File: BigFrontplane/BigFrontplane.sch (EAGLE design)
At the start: 7 parts

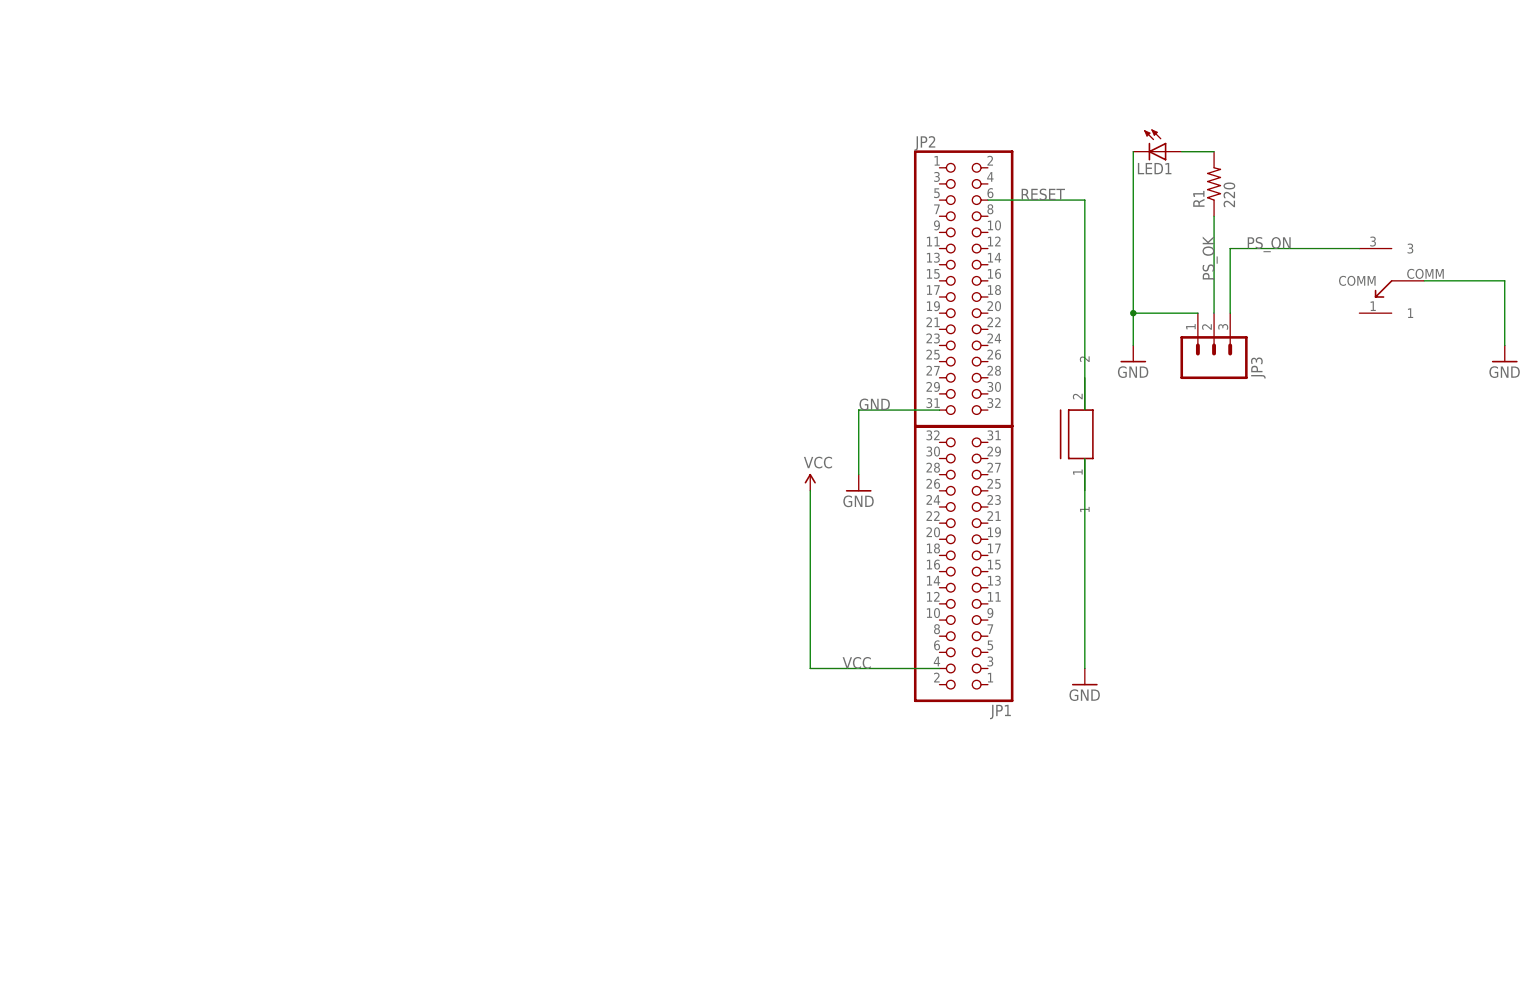
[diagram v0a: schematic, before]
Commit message: Updated Front Panel
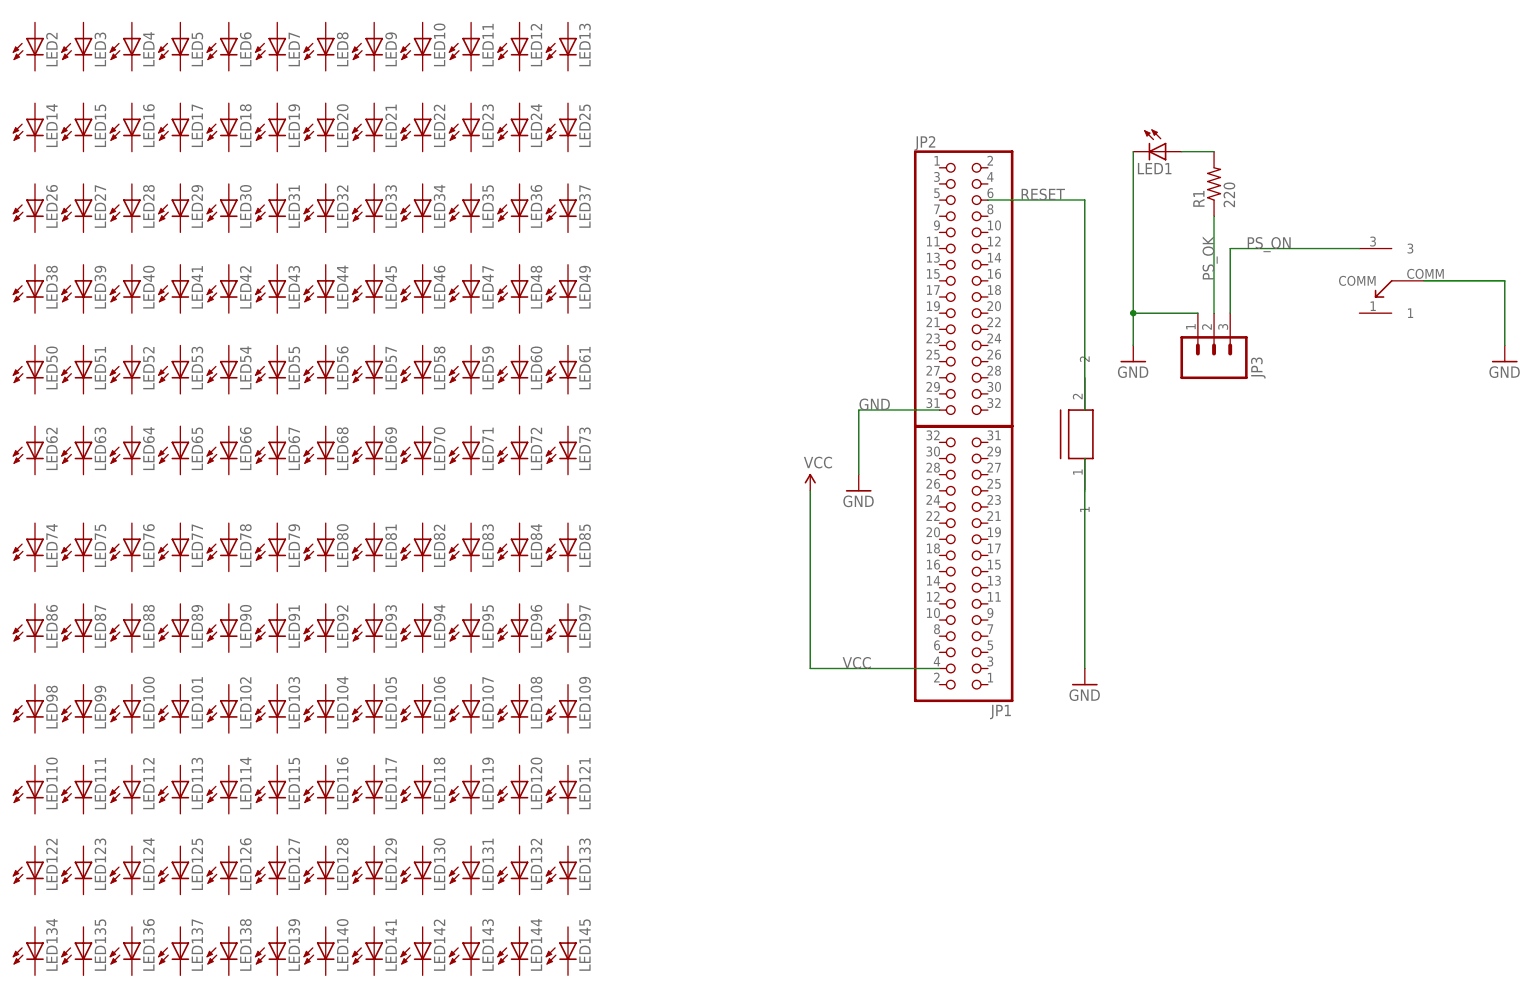
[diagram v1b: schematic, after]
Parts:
- added LED10, LED100, LED101, LED102, LED103, LED104, LED105, LED106, LED107, LED108, LED109, LED11, LED110, LED111, LED112, LED113, LED114, LED115, LED116, LED117, LED118, LED119, LED12, LED120, LED121, LED122, LED123, LED124, LED125, LED126, LED127, LED128, LED129, LED13, LED130, LED131, LED132, LED133, LED134, LED135, LED136, LED137, LED138, LED139, LED14, LED140, LED141, LED142, LED143, LED144, LED145, LED15, LED16, LED17, LED18, LED19, LED2, LED20, LED21, LED22, LED23, LED24, LED25, LED26, LED27, LED28, LED29, LED3, LED30, LED31, LED32, LED33, LED34, LED35, LED36, LED37, LED38, LED39, LED4, LED40, LED41, LED42, LED43, LED44, LED45, LED46, LED47, LED48, LED49, LED5, LED50, LED51, LED52, LED53, LED54, LED55, LED56, LED57, LED58, LED59, LED6, LED60, LED61, LED62, LED63, LED64, LED65, LED66, LED67, LED68, LED69, LED7, LED70, LED71, LED72, LED73, LED74, LED75, LED76, LED77, LED78, LED79, LED8, LED80, LED81, LED82, LED83, LED84, LED85, LED86, LED87, LED88, LED89, LED9, LED90, LED91, LED92, LED93, LED94, LED95, LED96, LED97, LED98, LED99: (no value), adafruit:LED3MM
